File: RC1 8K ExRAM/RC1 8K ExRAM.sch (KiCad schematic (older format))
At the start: 35 parts, among them J1 Expansion, J2 ADDRESS, J3 BATTERY, U1 74LS138, U2 74LS00, U3 74HC595, U4 74HC595, U5 HM62256BLP-7, U6 74LS244, U7 74LS244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

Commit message: Separate SRAM CS control
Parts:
- added R8: 3k3, Resistors_THT:R_Axial_DIN0207_L6.3mm_D2.5mm_P10.16mm_Horizontal, symbol Device:R
- D4: value 1n914 -> 1N4001
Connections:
- net GND: no longer U5.20 (~CS), U7.17 (I3b)
- net VCC: no longer R7.2
- net ~RC1_CS: now also U7.17 (I3b)
- net EX_~CS: now reaches U7.3 (O3b)
- net EX_~CS: now also A1.24 (A5), U5.20 (~CS), R8.1
- net SRAM_VCC renamed VMEM
- net VMEM: now also R7.2, R8.2
- no-connect marks 27 -> 25
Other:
- moved on the sheet: C5, D5, D6, J3
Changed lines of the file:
@@
 Entry Wire Line
 	10525 5325 10625 5425
-$Comp
-L power:GND #PWR06
-U 1 1 5D8144E9
-P 12475 6650
-F 0 "#PWR06" H 12475 6400 50  0001 C CNN
-F 1 "GND" H 12475 6500 50  0000 C CNN
-F 2 "" H 12475 6650 50  0001 C CNN
-F 3 "" H 12475 6650 50  0001 C CNN
-	1    12475 6650
-	1    0    0    -1
-$EndComp
 Wire Wire Line
 	12475 6650 12400 6650
@@
 Text Label 10650 6350 0    60   ~ 0
 EX_A12
-NoConn ~ 11000 6650
 Text GLabel 11000 8175 0    60   Input ~ 0
 ~RC1_CS
@@
 Wire Wire Line
 	12200 3525 12275 3525
-Wire Wire Line
-	12275 3525 12275 3775
-Wire Wire Line
-	12200 3775 12275 3775
-Connection ~ 12275 3775
 $Comp
 L power:GND #PWR07
@@
 NoConn ~ 6875 4025
 NoConn ~ 6875 4625
-NoConn ~ 6875 4725
 NoConn ~ 6875 4825
 NoConn ~ 7475 3225
@@
 Text Label 12525 3625 0    60   ~ 0
 EX_R/~W
-Wire Wire Line
-	12200 3625 12875 3625
 Entry Wire Line
 	12875 3625 12975 3725
@@
 P 7000 3075
 F 0 "D4" H 6950 3155 50  0000 L CNN
-F 1 "1n914" H 6850 2995 50  0000 L CNN
+F 1 "1N4001" H 6850 2995 50  0000 L CNN
 F 2 "Diodes_THT:D_DO-35_SOD27_P7.62mm_Horizontal" V 7000 3075 50  0001 C CNN
 F 3 "" V 7000 3075 50  0001 C CNN
@@
 Wire Wire Line
 	6625 3775 6625 3850
-Wire Wire Line
-	6225 3775 6425 3775
 Connection ~ 6425 3775
 Wire Wire Line
@@
 	6875 4425 6225 4425
 Wire Wire Line
-	6225 4150 6225 4425
-Wire Wire Line
-	6225 3850 6225 3775
-Wire Wire Line
 	6225 6050 8575 6050
-Connection ~ 6225 4425
 Entry Wire Line
 	8575 6050 8675 6150
@@
 	12475 5725 12550 5725
 Wire Wire Line
-	12275 3775 12275 3850
-Wire Wire Line
 	5850 6725 6800 6725
 Wire Wire Line
@@
 L Diode:1N4001 D5
 U 1 1 5F8B63C2
-P 12300 1525
-F 0 "D5" H 12300 1741 50  0000 C CNN
-F 1 "1N4001" H 12300 1650 50  0000 C CNN
-F 2 "Diodes_THT:D_DO-41_SOD81_P10.16mm_Horizontal" H 12300 1350 50  0001 C CNN
-F 3 "http://www.vishay.com/docs/88503/1n4001.pdf" H 12300 1525 50  0001 C CNN
-	1    12300 1525
+P 12300 1400
+F 0 "D5" H 12300 1616 50  0000 C CNN
+F 1 "1N4001" H 12300 1525 50  0000 C CNN
+F 2 "Diodes_THT:D_DO-41_SOD81_P10.16mm_Horizontal" H 12300 1225 50  0001 C CNN
+F 3 "http://www.vishay.com/docs/88503/1n4001.pdf" H 12300 1400 50  0001 C CNN
+	1    12300 1400
 	1    0    0    -1
 $EndComp
@@
 L conn:Conn_01x04 J3
 U 1 1 5F8DDE54
-P 12925 1800
-F 0 "J3" H 13005 1792 50  0000 L CNN
-F 1 "BATTERY" H 13005 1701 50  0000 L CNN
-F 2 "Pin_Headers:Pin_Header_Angled_1x04_Pitch2.54mm" H 12925 1800 50  0001 C CNN
-F 3 "~" H 12925 1800 50  0001 C CNN
-	1    12925 1800
-	1    0    0    -1
-$EndComp
-Wire Wire Line
-	12450 1700 12725 1700
-NoConn ~ 12725 1800
+P 12925 1675
+F 0 "J3" H 13005 1667 50  0000 L CNN
+F 1 "BATTERY" H 13005 1576 50  0000 L CNN
+F 2 "Pin_Headers:Pin_Header_Angled_1x04_Pitch2.54mm" H 12925 1675 50  0001 C CNN
+F 3 "~" H 12925 1675 50  0001 C CNN
+	1    12925 1675
+	1    0    0    -1
+$EndComp
+Wire Wire Line
+	12450 1575 12725 1575
+NoConn ~ 12725 1675
 $Comp
 L power:GND #PWR017
 U 1 1 5F92EA3F
-P 12650 2175
-F 0 "#PWR017" H 12650 1925 50  0001 C CNN
-F 1 "GND" H 12650 2025 50  0000 C CNN
-F 2 "" H 12650 2175 50  0001 C CNN
-F 3 "" H 12650 2175 50  0001 C CNN
-	1    12650 2175
-	1    0    0    -1
-$EndComp
-Wire Wire Line
-	12650 2000 12725 2000
-Wire Wire Line
-	12650 2000 12650 1900
-Wire Wire Line
-	12650 1900 12725 1900
+P 12650 2050
+F 0 "#PWR017" H 12650 1800 50  0001 C CNN
+F 1 "GND" H 12650 1900 50  0000 C CNN
+F 2 "" H 12650 2050 50  0001 C CNN
+F 3 "" H 12650 2050 50  0001 C CNN
+	1    12650 2050
+	1    0    0    -1
+$EndComp
+Wire Wire Line
+	12650 1875 12725 1875
+Wire Wire Line
+	12650 1875 12650 1775
+Wire Wire Line
+	12650 1775 12725 1775
 Wire Bus Line
 	12975 4425 10525 4425
 Connection ~ 10525 4425
 Wire Wire Line
-	12150 1525 11700 1525
+	12150 1400 11700 1400
 $Comp
 L power:VCC #PWR016
 U 1 1 5FB6267F
-P 12650 1450
-F 0 "#PWR016" H 12650 1300 50  0001 C CNN
-F 1 "VCC" H 12650 1600 50  0000 C CNN
-F 2 "" H 12650 1450 50  0001 C CNN
-F 3 "" H 12650 1450 50  0001 C CNN
-	1    12650 1450
-	1    0    0    -1
-$EndComp
-Wire Wire Line
-	12450 1525 12650 1525
-Wire Wire Line
-	12650 1525 12650 1450
-Wire Notes Line
-	13375 2350 13375 875
-Wire Notes Line
-	13375 875  11575 875
-Wire Notes Line
-	11575 875  11575 2350
-Wire Notes Line
-	11575 2350 13375 2350
+P 12650 1325
+F 0 "#PWR016" H 12650 1175 50  0001 C CNN
+F 1 "VCC" H 12650 1475 50  0000 C CNN
+F 2 "" H 12650 1325 50  0001 C CNN
+F 3 "" H 12650 1325 50  0001 C CNN
+	1    12650 1325
+	1    0    0    -1
+$EndComp
+Wire Wire Line
+	12450 1400 12650 1400
+Wire Wire Line
+	12650 1400 12650 1325
 Text Notes 11575 875  0    60   ~ 0
 External battery backup
 Text Notes 11625 1100 0    39   ~ 0
 Old school CMOS battery backup, use 3xAA batteries.\nShould utilize system power as long as it is available.\nUse pin 2 as a key indicator if possible.
-Text Label 12700 1700 2    39   ~ 0
+Text Label 12700 1575 2    39   ~ 0
 BATTERY
-Text Label 11700 2325 1    39   ~ 0
-SRAM_VCC
 Text Notes 11825 10575 0    60   ~ 0
 Revision B adds a battery pack that should keep data intact, this should function as long\nas the voltage does not exceed 4.5v.
@@
 L Diode:1N4001 D6
 U 1 1 5F8B70C2
-P 12300 1700
-F 0 "D6" H 12300 1916 50  0000 C CNN
-F 1 "1N4001" H 12300 1825 50  0000 C CNN
-F 2 "Diodes_THT:D_DO-41_SOD81_P10.16mm_Horizontal" H 12300 1525 50  0001 C CNN
-F 3 "http://www.vishay.com/docs/88503/1n4001.pdf" H 12300 1700 50  0001 C CNN
-	1    12300 1700
+P 12300 1575
+F 0 "D6" H 12300 1791 50  0000 C CNN
+F 1 "1N4001" H 12300 1700 50  0000 C CNN
+F 2 "Diodes_THT:D_DO-41_SOD81_P10.16mm_Horizontal" H 12300 1400 50  0001 C CNN
+F 3 "http://www.vishay.com/docs/88503/1n4001.pdf" H 12300 1575 50  0001 C CNN
+	1    12300 1575
 	1    0    0    1
 $EndComp
 Wire Wire Line
-	11700 1700 11700 1525
-Wire Wire Line
-	11700 1700 11700 2475
-Connection ~ 11700 1700
-Wire Wire Line
-	11700 1700 11975 1700
+	11700 1575 11700 1400
+Connection ~ 11700 1575
+Wire Wire Line
+	11700 1575 11975 1575
 $Comp
 L Device:C C5
 U 1 1 5D8412CC
-P 11975 1925
-F 0 "C5" H 12000 2025 50  0000 L CNN
-F 1 "100nF" H 12000 1825 50  0000 L CNN
-F 2 "Capacitors_THT:C_Disc_D4.7mm_W2.5mm_P5.00mm" H 12013 1775 50  0001 C CNN
-F 3 "" H 11975 1925 50  0001 C CNN
-	1    11975 1925
+P 11975 1800
+F 0 "C5" H 12000 1900 50  0000 L CNN
+F 1 "100nF" H 12000 1700 50  0000 L CNN
+F 2 "Capacitors_THT:C_Disc_D4.7mm_W2.5mm_P5.00mm" H 12013 1650 50  0001 C CNN
+F 3 "" H 11975 1800 50  0001 C CNN
+	1    11975 1800
 	-1   0    0    -1
 $EndComp
 Wire Wire Line
-	11975 1775 11975 1700
-Connection ~ 11975 1700
-Wire Wire Line
-	11975 1700 12150 1700
-Wire Wire Line
-	11975 2075 11975 2125
-Wire Wire Line
-	12650 2175 12650 2125
+	11975 1650 11975 1575
+Connection ~ 11975 1575
+Wire Wire Line
+	11975 1575 12150 1575
+Wire Wire Line
+	11975 1950 11975 2000
+Wire Wire Line
+	12650 2050 12650 2000
+Connection ~ 12650 1875
+Wire Wire Line
+	11975 2000 12650 2000
 Connection ~ 12650 2000
 Wire Wire Line
-	11975 2125 12650 2125
-Connection ~ 12650 2125
-Wire Wire Line
-	12650 2125 12650 2000
+	12650 2000 12650 1875
 Wire Wire Line
 	10475 10350 11025 10350
 Wire Wire Line
 	10475 10800 11025 10800
+Wire Notes Line
+	13375 2425 13375 875
+Wire Notes Line
+	11325 2425 11325 875
+Wire Wire Line
+	12275 3525 12275 3850
+Entry Wire Line
+	12875 3775 12975 3875
+Text Label 12525 3775 0    60   ~ 0
+EX_~CS
+$Comp
+L Device:R R8
+U 1 1 600BE1F4
+P 6025 4000
+F 0 "R8" V 6105 4000 50  0000 C CNN
+F 1 "3k3" V 6025 4000 50  0000 C CNN
+F 2 "Resistors_THT:R_Axial_DIN0207_L6.3mm_D2.5mm_P10.16mm_Horizontal" V 5955 4000 50  0001 C CNN
+F 3 "" H 6025 4000 50  0001 C CNN
+	1    6025 4000
+	-1   0    0    1
+$EndComp
+Wire Wire Line
+	6225 4150 6225 4425
+Connection ~ 6225 4425
+Wire Wire Line
+	12200 3625 12875 3625
+Wire Wire Line
+	12200 3775 12875 3775
+Wire Wire Line
+	11700 1575 11700 2475
+Connection ~ 11700 1400
+Wire Wire Line
+	6225 3700 6225 3775
+Wire Wire Line
+	6875 4725 6025 4725
+Wire Wire Line
+	6025 4725 6025 4150
+Wire Wire Line
+	6225 3775 6025 3775
+Wire Wire Line
+	6025 3775 6025 3850
+Connection ~ 6225 3775
+Wire Wire Line
+	6225 3775 6225 3850
+Wire Wire Line
+	6025 4725 6025 6150
+Wire Wire Line
+	6025 6150 8575 6150
+Connection ~ 6025 4725
+Entry Wire Line
+	8575 6150 8675 6250
+Text Label 8550 6150 2    60   ~ 0
+EX_~CS
+Wire Wire Line
+	11600 1400 11700 1400
+Wire Notes Line
+	11325 2425 13375 2425
+Wire Notes Line
+	11325 875  13375 875
+Text Label 11700 2400 1    39   ~ 0
+STANDBY
+Text Label 10650 6650 0    60   ~ 0
+EX_~CS
+Wire Wire Line
+	12475 6650 12475 6850
+Connection ~ 12475 6850
+Wire Wire Line
+	11000 6650 10625 6650
+Entry Wire Line
+	10625 6650 10525 6750
+$Comp
+L power:VMEM #PWR0101
+U 1 1 60B3EED7
+P 11600 1400
+F 0 "#PWR0101" H 11600 1250 50  0001 C CNN
+F 1 "VMEM" V 11615 1528 50  0000 L CNN
+F 2 "" H 11600 1400 50  0001 C CNN
+F 3 "" H 11600 1400 50  0001 C CNN
+	1    11600 1400
+	0    -1   -1   0
+$EndComp
+$Comp
+L power:VMEM #PWR0102
+U 1 1 60B402ED
+P 6225 3700
+F 0 "#PWR0102" H 6225 3550 50  0001 C CNN
+F 1 "VMEM" H 6125 3850 50  0000 L CNN
+F 2 "" H 6225 3700 50  0001 C CNN
+F 3 "" H 6225 3700 50  0001 C CNN
+	1    6225 3700
+	1    0    0    -1
+$EndComp
 Wire Bus Line
 	825  600  825  2300

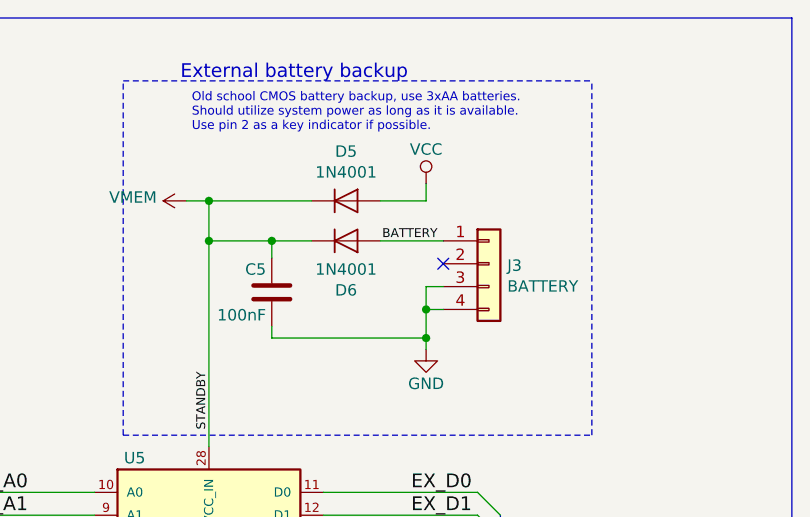
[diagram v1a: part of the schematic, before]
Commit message: Updated schematic to match prototype
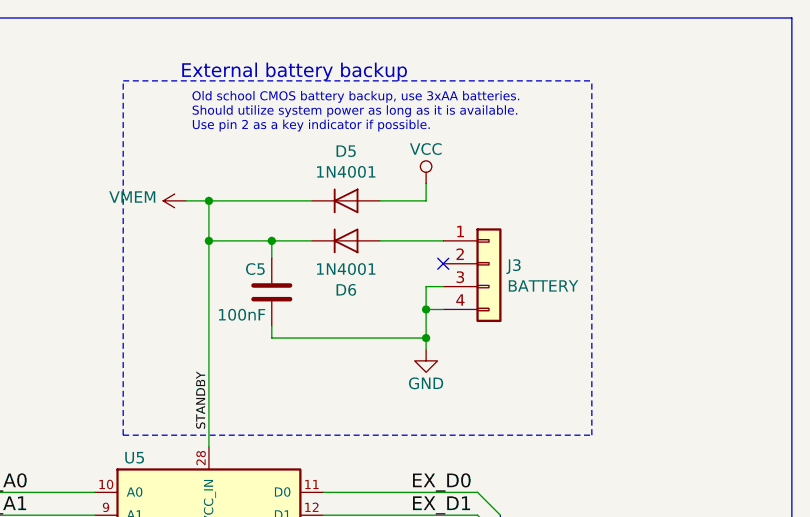
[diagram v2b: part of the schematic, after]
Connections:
- net BATTERY: no longer names the net of D6.2 (A), J3.1 (Pin_1)
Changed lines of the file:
@@
 Text Notes 11625 1100 0    39   ~ 0
 Old school CMOS battery backup, use 3xAA batteries.\nShould utilize system power as long as it is available.\nUse pin 2 as a key indicator if possible.
-Text Label 12700 1575 2    39   ~ 0
-BATTERY
 Text Notes 11825 10575 0    60   ~ 0
 Revision B adds a battery pack that should keep data intact, this should function as long\nas the voltage does not exceed 4.5v.
@@
 Connection ~ 11700 1400
 Wire Wire Line
-	6225 3700 6225 3775
-Wire Wire Line
 	6875 4725 6025 4725
 Wire Wire Line
@@
 Text Label 8550 6150 2    60   ~ 0
 EX_~CS
-Wire Wire Line
-	11600 1400 11700 1400
 Wire Notes Line
 	11325 2425 13375 2425
@@
 Entry Wire Line
 	10625 6650 10525 6750
+Wire Wire Line
+	11600 1400 11700 1400
+Wire Wire Line
+	6225 3700 6225 3775
+Wire Bus Line
+	8675 2400 8675 8325
+Wire Bus Line
+	10525 4425 10525 7775
+Wire Bus Line
+	12975 4650 12975 8325
+Wire Bus Line
+	12975 2775 12975 4425
+Wire Bus Line
+	10525 2400 10525 4425
+Wire Bus Line
+	825  600  825  2300
+Wire Bus Line
+	14250 600  14250 8675
+$Comp
+L power:VMEM #PWR0102
+U 1 1 60B402ED
+P 6225 3700
+F 0 "#PWR0102" H 6225 3550 50  0001 C CNN
+F 1 "VMEM" H 6125 3850 50  0000 L CNN
+F 2 "" H 6225 3700 50  0001 C CNN
+F 3 "" H 6225 3700 50  0001 C CNN
+	1    6225 3700
+	1    0    0    -1
+$EndComp
 $Comp
 L power:VMEM #PWR0101
@@
 	0    -1   -1   0
 $EndComp
-$Comp
-L power:VMEM #PWR0102
-U 1 1 60B402ED
-P 6225 3700
-F 0 "#PWR0102" H 6225 3550 50  0001 C CNN
-F 1 "VMEM" H 6125 3850 50  0000 L CNN
-F 2 "" H 6225 3700 50  0001 C CNN
-F 3 "" H 6225 3700 50  0001 C CNN
-	1    6225 3700
-	1    0    0    -1
-$EndComp
-Wire Bus Line
-	825  600  825  2300
-Wire Bus Line
-	12975 2775 12975 4425
-Wire Bus Line
-	10525 4425 10525 7775
-Wire Bus Line
-	10525 2400 10525 4425
-Wire Bus Line
-	14250 600  14250 8675
-Wire Bus Line
-	12975 4650 12975 8325
-Wire Bus Line
-	8675 2400 8675 8325
 $EndSCHEMATC
